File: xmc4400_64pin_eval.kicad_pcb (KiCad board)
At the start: 4 copper layers, 60 x 30 mm, 47 parts, among them IC1 TLV75533PDBVR, IC2 SN65HVD230DR, J1 VCP, J2 SWD & JTAG, J3 IO_1, J4 IO_2, J5 POW, J6 CAN, J7 Vbat, U1 XMC440x-LQFP64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

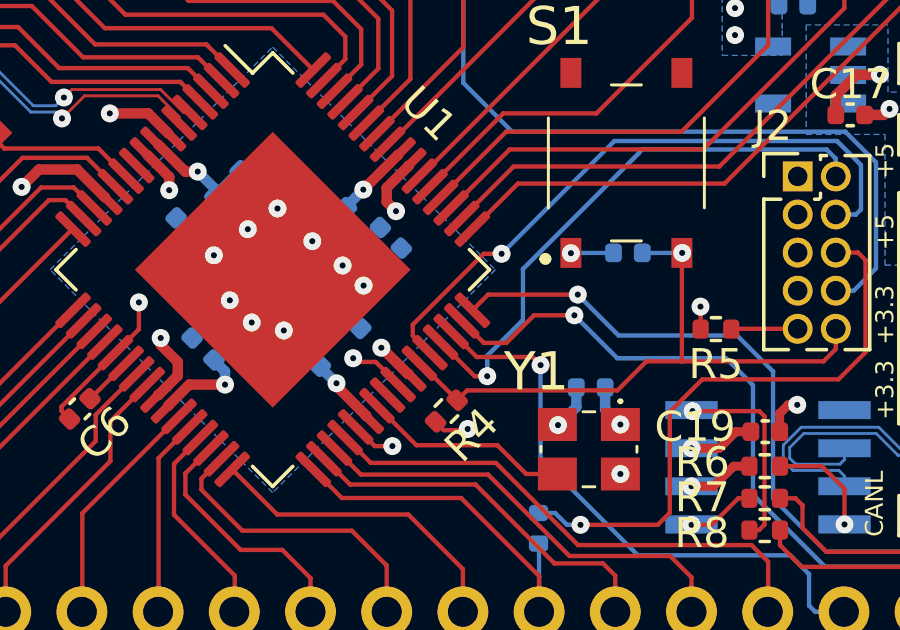
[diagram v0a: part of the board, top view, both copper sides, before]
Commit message: Fix swd pins
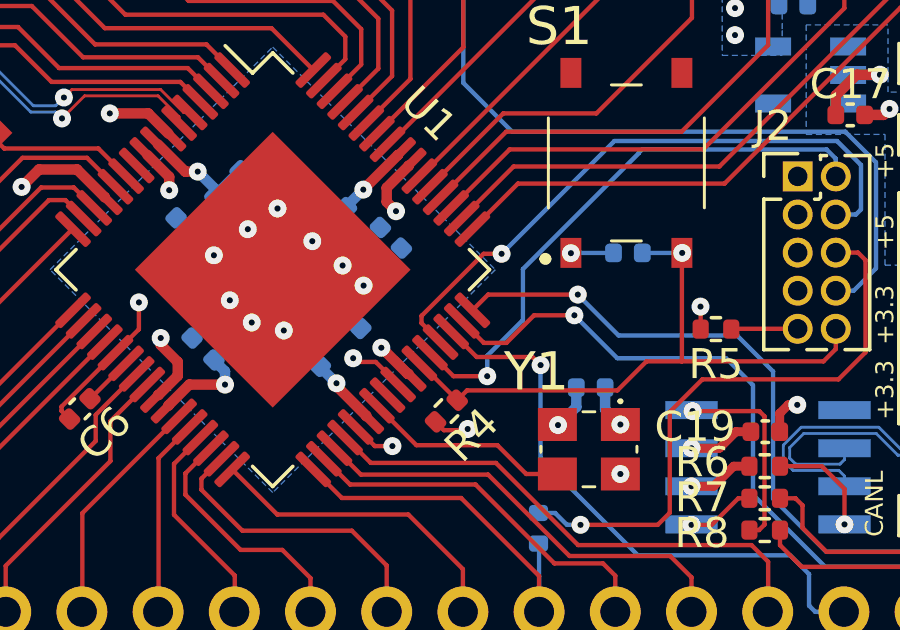
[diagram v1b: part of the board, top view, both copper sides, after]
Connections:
- U1 pad 44: XMC_TCK/SWCLK -> XMC_TMS/SWDIO
- U1 pad 45: XMC_TMS/SWDIO -> XMC_TCK/SWCLK
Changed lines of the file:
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@@
       (net 6 "XMC_RESET") (pinfunction "PORST") (pintype "input"))
     (pad "44" smd roundrect (at 5.6625 -1.75 315) (size 1.475 0.3) (layers "F.Cu" "F.Paste" "F.Mask") (roundrect_rratio 0.25)
-      (net 17 "XMC_TCK{slash}SWCLK") (pinfunction "TMS/SWCLK") (pintype "bidirectional"))
+      (net 16 "XMC_TMS{slash}SWDIO") (pinfunction "TMS/SWDIO") (pintype "bidirectional"))
     (pad "45" smd roundrect (at 5.6625 -2.25 315) (size 1.475 0.3) (layers "F.Cu" "F.Paste" "F.Mask") (roundrect_rratio 0.25)
-      (net 16 "XMC_TMS{slash}SWDIO") (pinfunction "TCK/SWDIO") (pintype "bidirectional"))
+      (net 17 "XMC_TCK{slash}SWCLK") (pinfunction "TCK/SWCLK") (pintype "bidirectional"))
     (pad "46" smd roundrect (at 5.6625 -2.75 315) (size 1.475 0.3) (layers "F.Cu" "F.Paste" "F.Mask") (roundrect_rratio 0.25)
       (net 52 "P1_15") (pinfunction "P1.15") (pintype "bidirectional"))
@@
   (via (at 33.36 52.12) (size 0.6) (drill 0.2) (layers "F.Cu" "B.Cu") (net 15))
   (via (at 33.5 47.46) (size 0.6) (drill 0.2) (layers "F.Cu" "B.Cu") (net 15))
-  (segment (start 67.634982 48.733002) (end 68.77198 49.87) (width 0.146812) (layer "F.Cu") (net 16))
-  (segment (start 68.77198 49.87) (end 69.19 49.87) (width 0.146812) (layer "F.Cu") (net 16))
+  (segment (start 67.276555 49.086555) (end 67.281429 49.086555) (width 0.146812) (layer "F.Cu") (net 16))
+  (segment (start 68.064874 49.87) (end 67.281429 49.086555) (width 0.146812) (layer "F.Cu") (net 16))
+  (segment (start 69.19 49.87) (end 68.064874 49.87) (width 0.146812) (layer "F.Cu") (net 16))
   (via (at 69.19 49.87) (size 0.6) (drill 0.2) (layers "F.Cu" "B.Cu") (net 16))
   (segment (start 74.25 42.413624) (end 74.25 42.43) (width 0.146812) (layer "B.Cu") (net 16))
@@
   (segment (start 80.5 42.31) (end 74.353624 42.31) (width 0.146812) (layer "B.Cu") (net 16))
   (segment (start 69.67 45.79) (end 69.07 45.79) (width 0.146812) (layer "F.Cu") (net 17))
-  (segment (start 67.276555 49.086555) (end 67.281429 49.086555) (width 0.146812) (layer "F.Cu") (net 17))
-  (segment (start 66.71 48.52) (end 67.276555 49.086555) (width 0.146812) (layer "F.Cu") (net 17))
-  (segment (start 69.07 45.79) (end 66.71 48.15) (width 0.146812) (layer "F.Cu") (net 17))
-  (segment (start 66.71 48.15) (end 66.71 48.52) (width 0.146812) (layer "F.Cu") (net 17))
+  (segment (start 69.07 45.79) (end 67.02 47.84) (width 0.146812) (layer "F.Cu") (net 17))
+  (segment (start 67 48.1) (end 67 47.86) (width 0.146812) (layer "F.Cu") (net 17))
+  (segment (start 67.633002 48.733002) (end 67 48.1) (width 0.146812) (layer "F.Cu") (net 17))
+  (segment (start 67 47.86) (end 67.02 47.84) (width 0.146812) (layer "F.Cu") (net 17))
+  (segment (start 67.634982 48.733002) (end 67.633002 48.733002) (width 0.146812) (layer "F.Cu") (net 17))
   (via (at 69.67 45.79) (size 0.6) (drill 0.2) (layers "F.Cu" "B.Cu") (net 17))
   (segment (start 81.65 44.31) (end 81.48 44.48) (width 0.146812) (layer "B.Cu") (net 17))
